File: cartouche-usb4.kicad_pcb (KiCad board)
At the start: 4 copper layers, 30 x 63.8 mm, 135 parts, among them CN1 M.2-MKEY CONNECTOR, J17 ?HDR1x1, J18 ?HDR1x1, U01 LTC3315AEV#TRPBF, U02 TPS82130SILR, U2 ASM2464PD, U31 ZD25WQ16CEIGR, U4 SIP32408DNP-T1-GE4, X1 25MHz

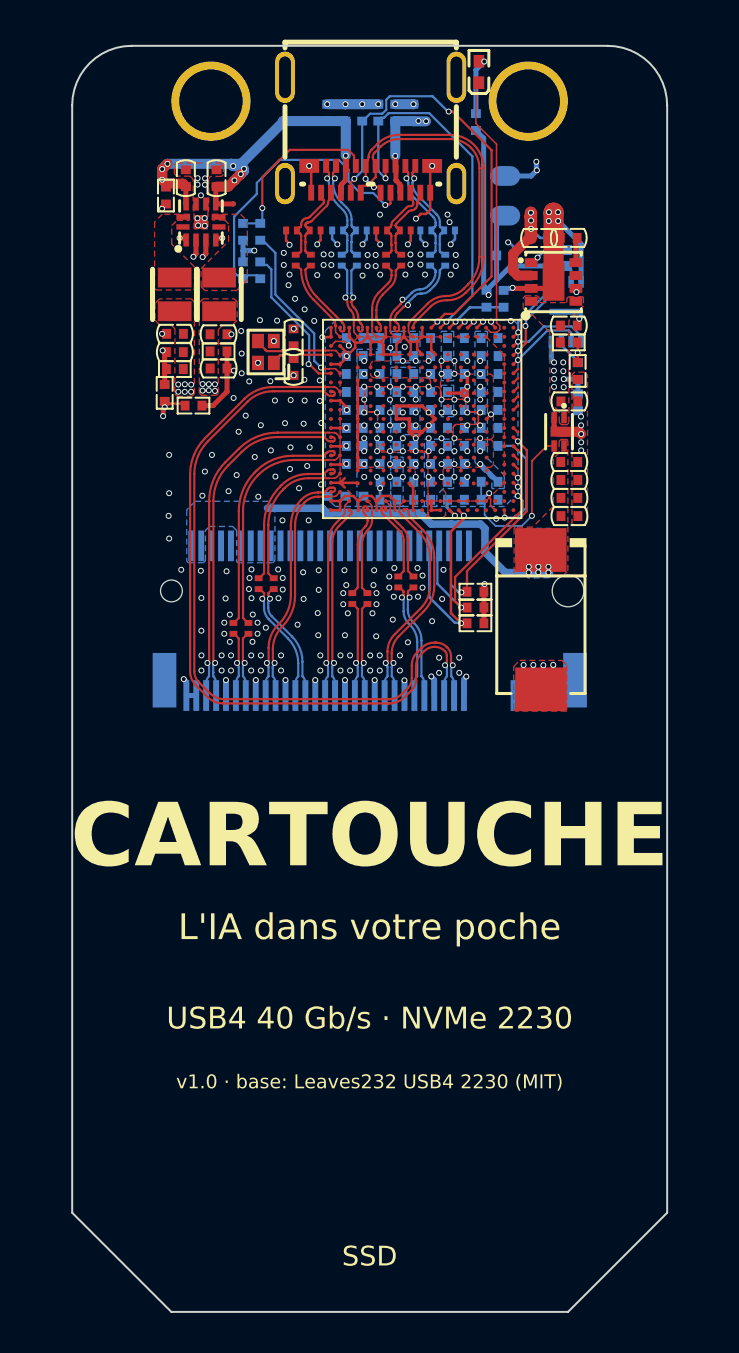
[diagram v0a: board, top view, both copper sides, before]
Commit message: v1.1: smallest possible board (22.0 x 33.7 mm) for a closed case
The name is engraved on the case, not printed on the board; the case holds the
SSD. Keeps the original proven outline. Adds a STEP model to design the case,
Gerbers with separate plated/non-plated drills, updated renders and README.
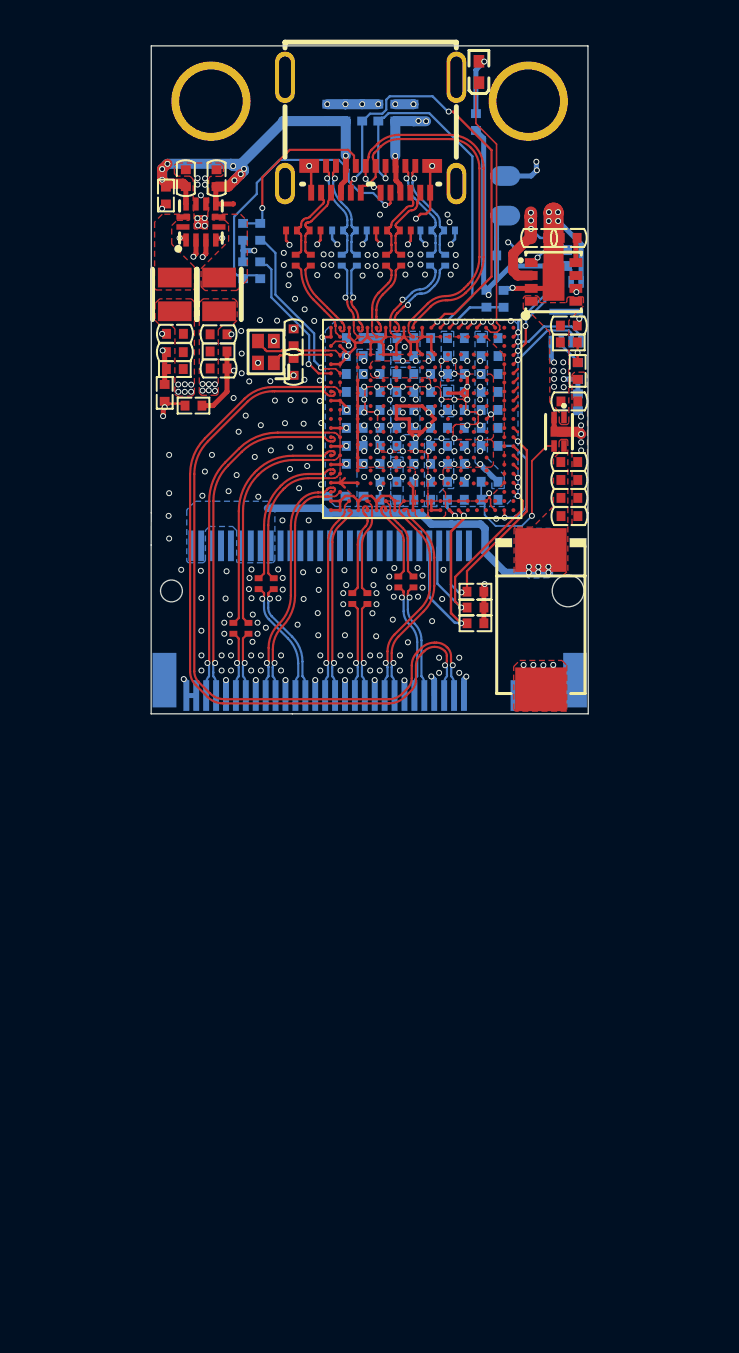
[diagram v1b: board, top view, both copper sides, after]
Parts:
- removed H1: M2 SSD 2230, 
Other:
- board size 30 x 63.8 mm -> 22 x 33.7 mm
- board text removed: "CARTOUCHE"
- board text removed: "L'IA dans votre poche"
- board text removed: "SSD"
- board text removed: "USB4 40 Gb/s · NVMe 2230"
- board text removed: "v1.0 · base: Leaves232 USB4 2230 (MIT)"
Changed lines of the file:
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@@
 		(embedded_fonts no)
 	)
-	(footprint ""
-		(layer "F.Cu")
-		(at 148.5 145)
-		(property "Reference" "H1"
-			(at 0 0 0)
-			(layer "F.Fab")
-			(effects
-				(font
-					(size 1.27 1.27)
-					(thickness 0.15)
-				)
-			)
-		)
-		(property "Value" "M2 SSD 2230"
-			(at 0 0 0)
-			(layer "F.Fab")
-			(effects
-				(font
-					(size 1.27 1.27)
-					(thickness 0.15)
-				)
-			)
-		)
-		(property "Datasheet" ""
-			(at 0 0 0)
-			(layer "F.Fab")
-			(hide yes)
-			(effects
-				(font
-					(size 1.27 1.27)
-					(thickness 0.15)
-				)
-			)
-		)
-		(property "Description" ""
-			(at 0 0 0)
-			(layer "F.Fab")
-			(hide yes)
-			(effects
-				(font
-					(size 1.27 1.27)
-					(thickness 0.15)
-				)
-			)
-		)
-		(pad "" np_thru_hole oval
-			(at 0 0)
-			(size 2.2 6.2)
-			(drill oval 2.2 6.2)
-			(layers "*.Cu" "*.Mask")
-			(thermal_bridge_angle 45)
-		)
-		(embedded_fonts no)
-	)
 	(footprint "ASM2464PD:R0402"
 		(layer "F.Cu")
@@
 	)
 	(gr_line
-		(start 158.5 152)
-		(end 138.5 152)
+		(start 144.600005 121.843815)
+		(end 137.481195 121.843815)
 		(stroke
-			(width 0.1)
-			(type default)
+			(width 0.05)
+			(type solid)
 		)
 		(layer "Edge.Cuts")
 	)
 	(gr_line
-		(start 163.5 147)
-		(end 158.5 152)
+		(start 159.521005 111.705405)
+		(end 159.521005 121.843265)
 		(stroke
-			(width 0.1)
-			(type default)
+			(width 0.05)
+			(type solid)
 		)
 		(layer "Edge.Cuts")
 	)
-	(gr_arc
-		(start 133.5 91.16)
-		(mid 134.37868 89.03868)
-		(end 136.5 88.16)
+	(gr_line
+		(start 159.521005 121.843265)
+		(end 144.600005 121.843815)
 		(stroke
-			(width 0.1)
-			(type default)
+			(width 0.05)
+			(type solid)
 		)
 		(layer "Edge.Cuts")
 	)
 	(gr_line
-		(start 163.5 91.16)
-		(end 163.5 147)
+		(start 137.481195 113.331925)
+		(end 137.487445 111.705405)
 		(stroke
-			(width 0.1)
-			(type default)
+			(width 0.05)
+			(type solid)
 		)
 		(layer "Edge.Cuts")
 	)
 	(gr_line
-		(start 138.5 152)
-		(end 133.5 147)
+		(start 137.487445 111.705405)
+		(end 137.487445 88.163385)
 		(stroke
-			(width 0.1)
-			(type default)
+			(width 0.05)
+			(type solid)
 		)
 		(layer "Edge.Cuts")
 	)
 	(gr_line
-		(start 133.5 147)
-		(end 133.5 91.16)
+		(start 137.481195 121.843815)
+		(end 137.481195 113.331925)
 		(stroke
-			(width 0.1)
-			(type default)
+			(width 0.05)
+			(type solid)
 		)
 		(layer "Edge.Cuts")
 	)
-	(gr_arc
-		(start 160.5 88.16)
-		(mid 162.62132 89.03868)
-		(end 163.5 91.16)
+	(gr_line
+		(start 159.507365 111.705405)
+		(end 159.521005 111.705405)
 		(stroke
-			(width 0.1)
-			(type default)
+			(width 0.05)
+			(type solid)
 		)
 		(layer "Edge.Cuts")
 	)
 	(gr_line
-		(start 136.5 88.16)
-		(end 160.5 88.16)
+		(start 137.487445 88.163385)
+		(end 159.507365 88.163385)
 		(stroke
-			(width 0.1)
-			(type default)
+			(width 0.05)
+			(type solid)
 		)
 		(layer "Edge.Cuts")
 	)
-	(gr_text "v1.0 · base: Leaves232 USB4 2230 (MIT)"
-		(at 148.5 140.4 0)
-		(layer "F.SilkS")
-		(effects
-			(font
-				(size 0.7 0.7)
-				(thickness 0.105)
-			)
-		)
-	)
-	(gr_text "SSD"
-		(at 148.5 149.2 0)
-		(layer "F.SilkS")
-		(effects
-			(font
-				(size 1 1)
-				(thickness 0.15)
-			)
-		)
-	)
-	(gr_text "L'IA dans votre poche"
-		(at 148.5 132.6 0)
-		(layer "F.SilkS")
-		(effects
-			(font
-				(size 1.3 1.3)
-				(thickness 0.195)
-			)
-		)
-	)
-	(gr_text "USB4 40 Gb/s · NVMe 2230"
-		(at 148.5 137.2 0)
-		(layer "F.SilkS")
-		(effects
-			(font
-				(size 1.1 1.1)
-				(thickness 0.165)
-			)
-		)
-	)
-	(gr_text "CARTOUCHE"
-		(at 148.5 128 0)
-		(layer "F.SilkS")
-		(effects
-			(font
-				(size 3.2 3.2)
-				(thickness 0.64)
-				(bold yes)
-			)
+	(gr_line
+		(start 159.507365 88.163385)
+		(end 159.507365 111.705405)
+		(stroke
+			(width 0.05)
+			(type solid)
 		)
+		(layer "Edge.Cuts")
 	)
 	(gr_text ""
